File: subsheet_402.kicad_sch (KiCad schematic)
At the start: 39 parts, among them J400 DIN-13S — Video Port, Q400 2N3904, Q401 2N3904, Q402 2N3904, Q403 2N3904, U405 74S257_PHY

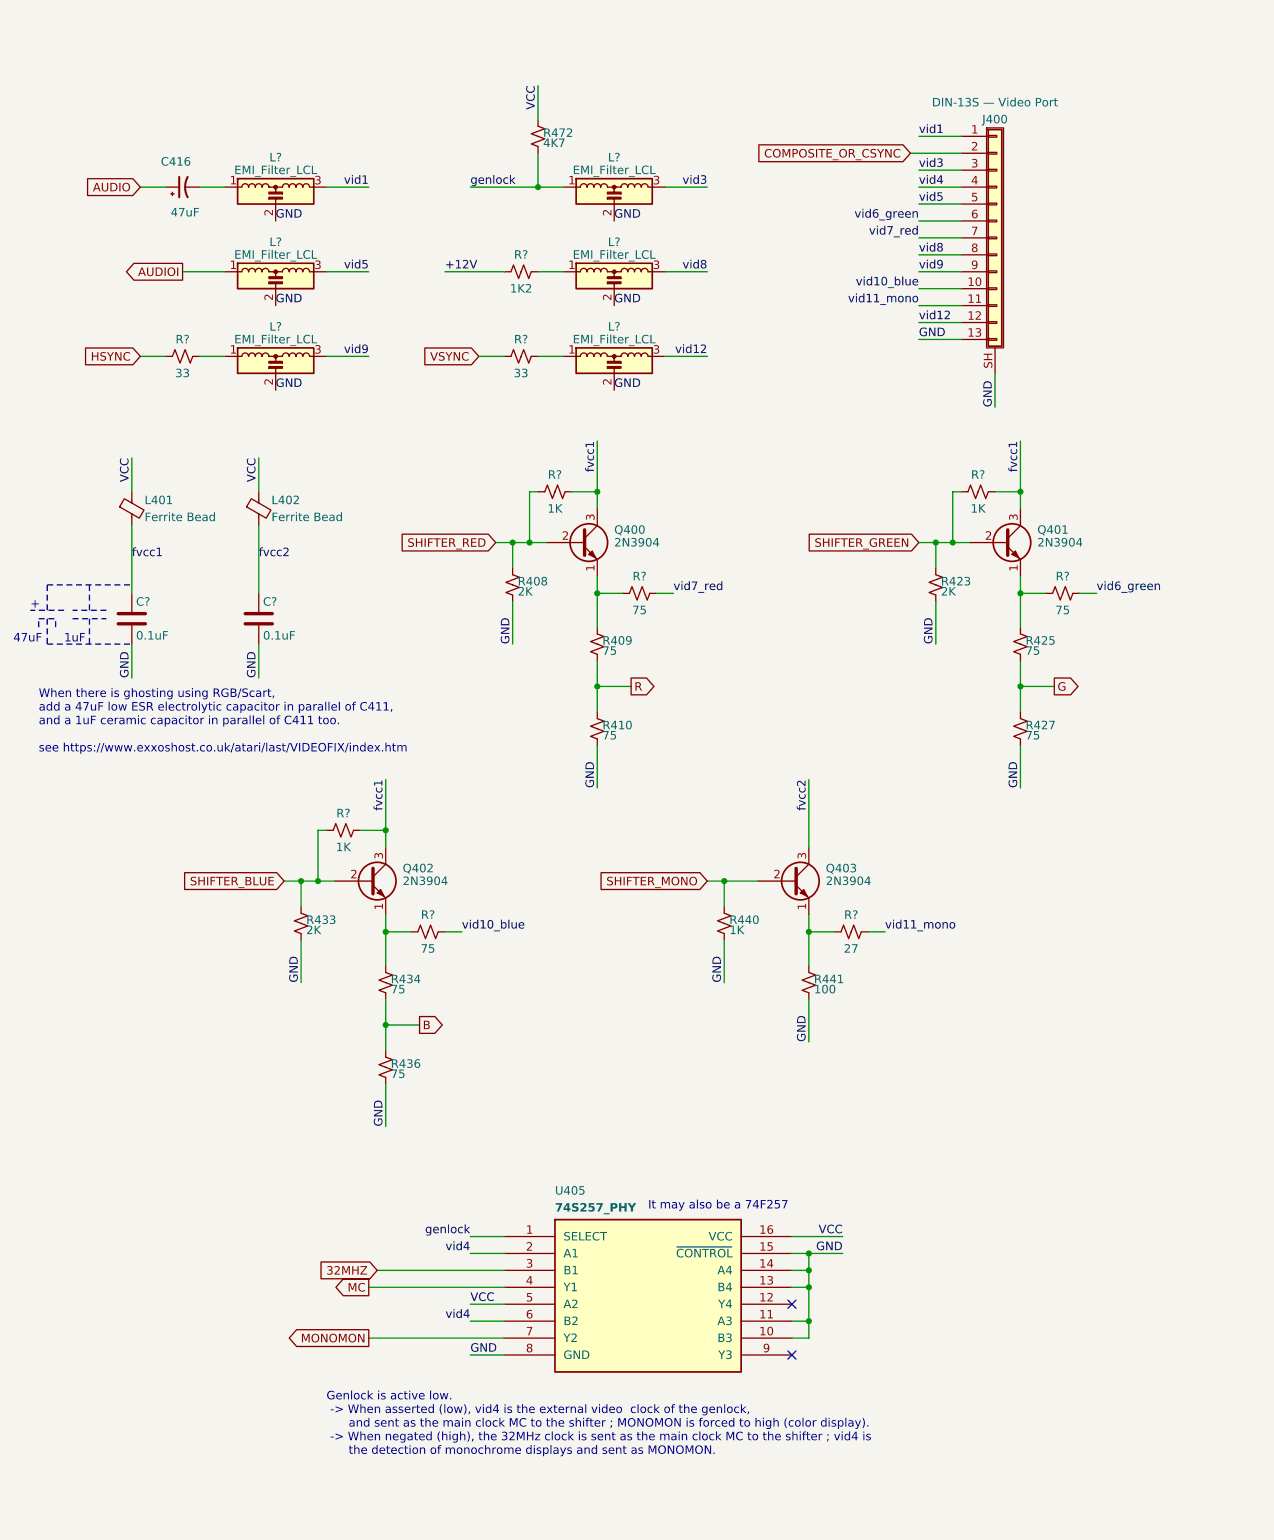
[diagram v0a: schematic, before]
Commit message: Resolves #3 : [schematic] annotate video port with signal name
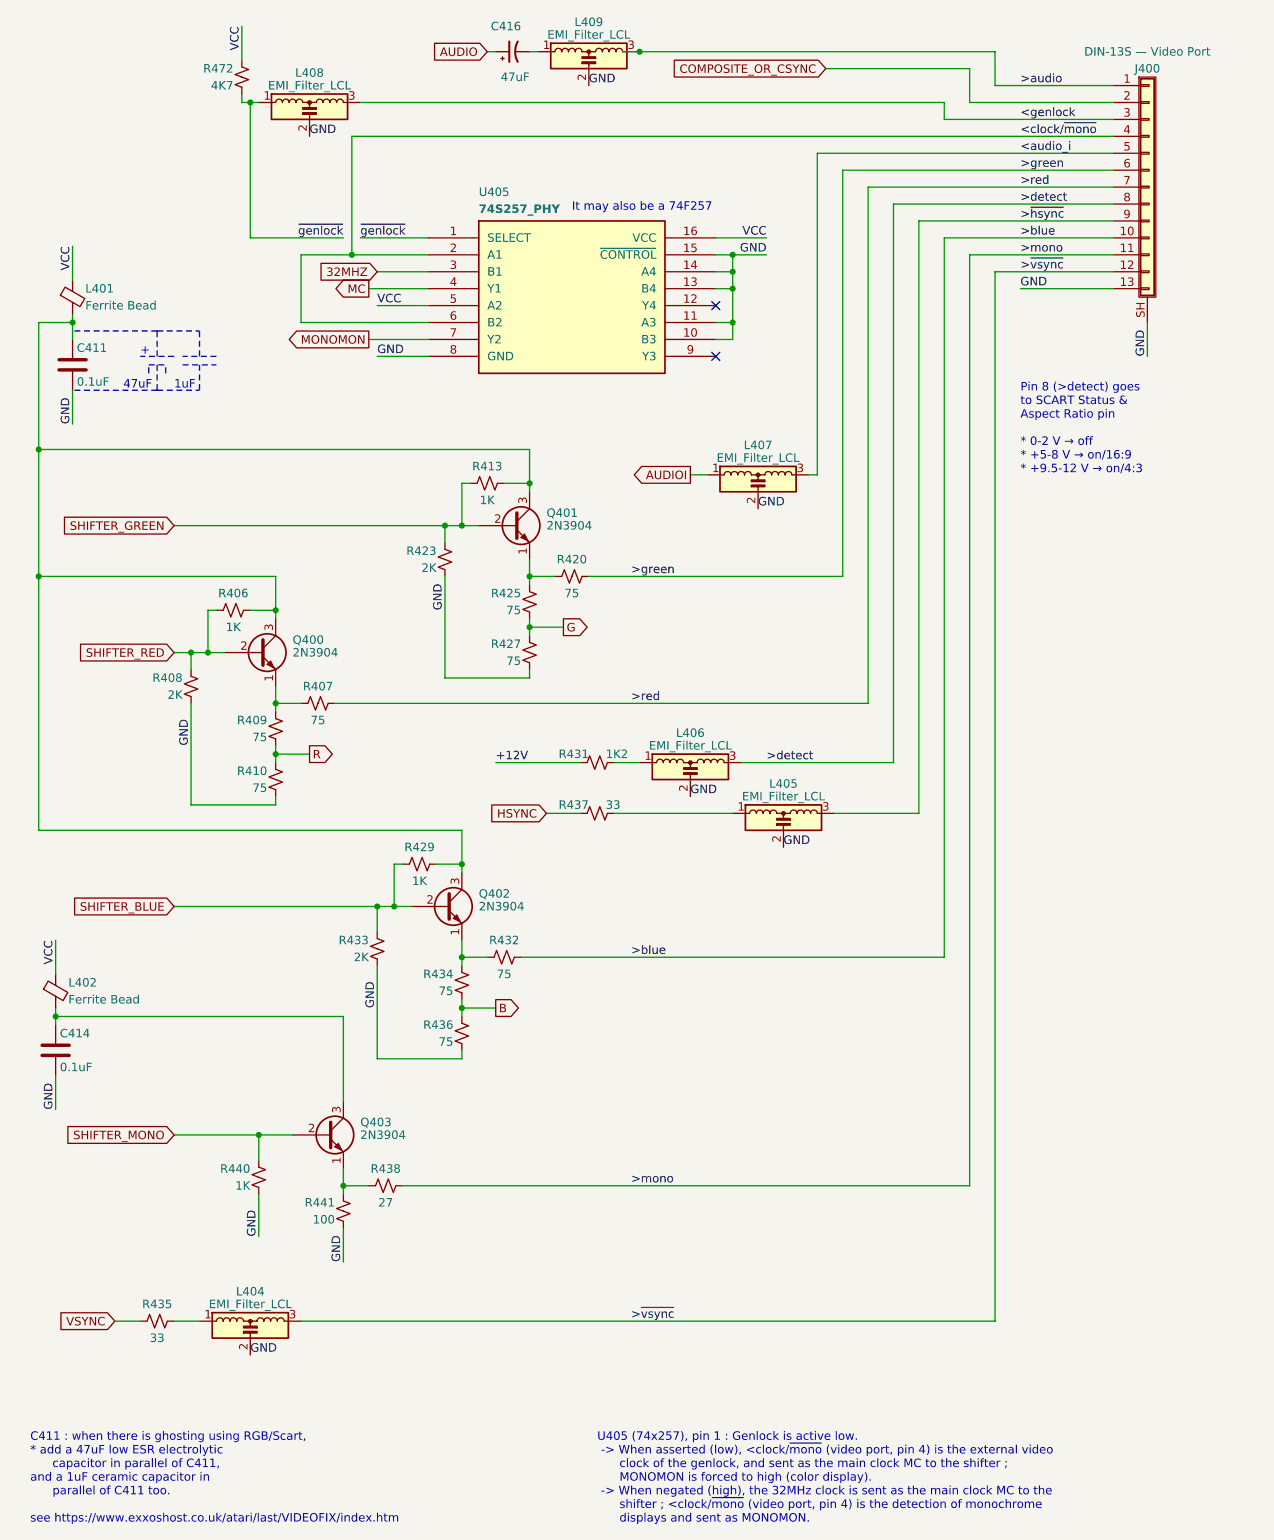
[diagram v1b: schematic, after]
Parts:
- gave numbers to parts that had none: 18
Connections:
- net fvcc1: no longer names the net of C411.1, L401.2, Q400.3 (C), Q401.3 (C), Q402.3 (C), R406.1, R413.1, R429.1
- net fvcc2: no longer names the net of C414.1, L402.2, Q403.3 (C)
- net genlock renamed ~{genlock}
- net vid1 renamed >audio
- net vid10_blue renamed >blue
- net vid11_mono renamed >mono
- net vid12 renamed >~{vsync}
- net vid3 renamed <genlock
- net vid4 renamed <clock/~{mono}
- net vid5 renamed <audio_i
- net vid6_green renamed >green
- net vid7_red renamed >red
- net vid8 renamed >detect
- net vid9 renamed >~{hsync}
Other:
- note added: "C411 : when there is ghosting using RGB/Scart, * add a 47uF low ESR electrolytic capacitor in parallel of C411, and a 1uF ceramic capacitor in parallel of C411 too. see https://www.exxoshost.co.uk/atari/last/VIDEOFIX/index.htm"
- note added: "Pin 8 (>detect) goes to SCART Status & Aspect Ratio pin * 0-2 V → off * +5-8 V → on/16:9 * +9.5-12 V → on/4:3"
- note added: "U405 (74x257), pin 1 : Genlock is active low. -> When asserted (low), <clock/~{mono} (video port, pin 4) is the external video clock of the genlock, and sent as the main clock MC to the shifter ; MONOMON is forced to high (color display). -> When negated (high), the 32MHz clock is sent as the main clock MC to the shifter ; <clock/~{mono} (video port, pin 4) is the detection of monochrome displays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"
- note removed: "Genlock is active low. -> When asserted (low), vid4 is the external video clock of the genlock, and sent as the main clock MC to the shifter ; MONOMON is forced to high (color display). -> When negated (high), the 32MHz clock is sent as the main clock MC to the shifter ; vid4 is the detection of monochrome displays and sent as MONOMON."
- note removed: "When there is ghosting using RGB/Scart, add a 47uF low ESR electrolytic capacitor in parallel of C411, and a 1uF ceramic capacitor in parallel of C411 too. see https://www.exxoshost.co.uk/atari/last/VIDEOFIX/index.htm"
- moved on the sheet: C411, C414, C416, J400, L401, L402, L404, L405, L406, L407, L408, L409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
